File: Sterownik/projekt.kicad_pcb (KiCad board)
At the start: 2 copper layers, 55.9 x 45.7 mm, 61 parts, among them P1 CONN_01X08, P3 CONN_01X05, P4 CONN_01X02, P5 CONN_01X02, P6 USB_OTG, P8 CONN_01X02, SW1 SW_PUSH_SMALL, T10 Si2323DS, T12 2N7002, T18 2N7002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

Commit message: More fixes and new trace placing
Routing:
- net MAIN_VOL: track 62.5 -> 48.2 mm
- net VBUS: track 110.1 -> 119.5 mm
- net GND: track 744.3 -> 740.8 mm, vias 136 -> 138
- net CHARGE_STAT: track 31.8 -> 28.8 mm
- net VDD: track 211.6 -> 214.1 mm
- net CHARGE_ENABLE: track 32.2 -> 32.9 mm

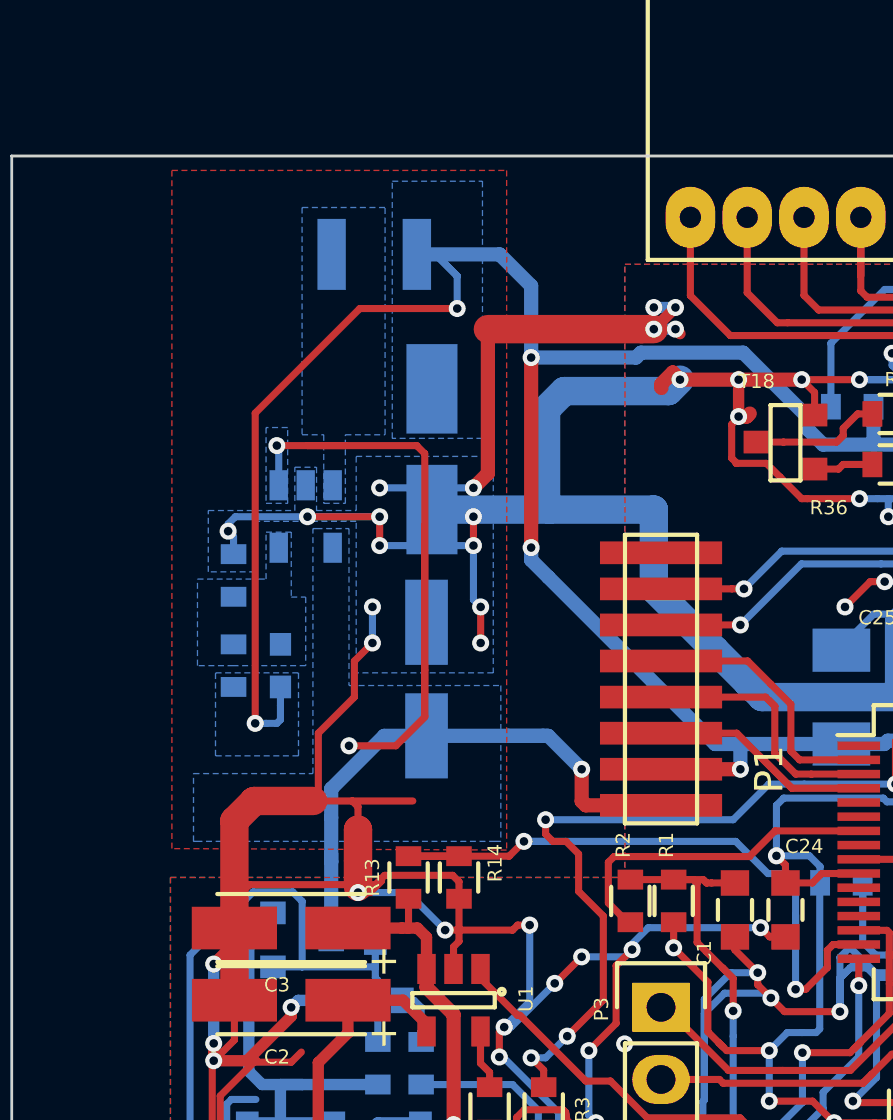
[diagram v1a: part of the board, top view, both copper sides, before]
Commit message: DC/DC converter to linear converter change
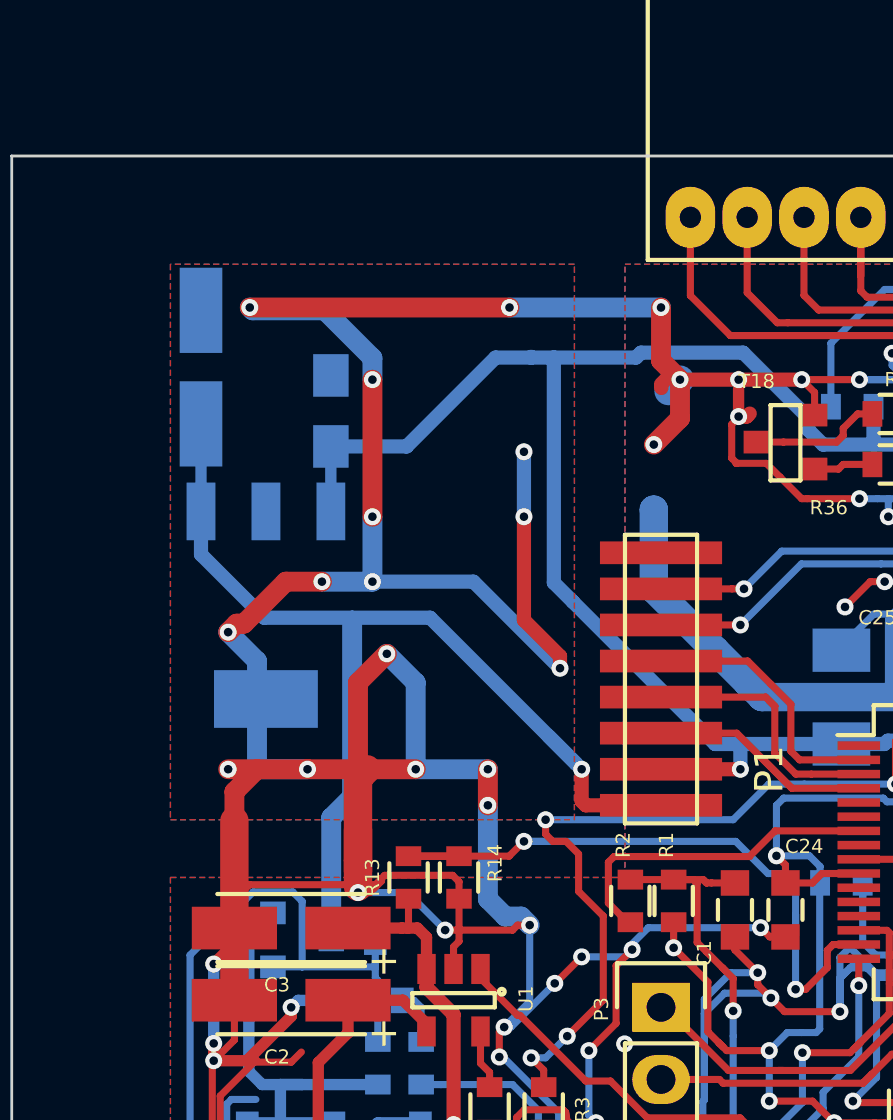
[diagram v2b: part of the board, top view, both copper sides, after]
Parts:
- removed C5: 22p, Capacitors_SMD:C_0603
- removed L2: NLCV32T-1R0M-PF, Capacitors_SMD:C_1210
- removed R18: 300K, Resistors_SMD:R_0603
- removed R20: 1,35M, Resistors_SMD:R_0603
- C6: value 10u -> 1U; footprint Capacitors_Tantalum_SMD:TantalC_SizeB_EIA-3528_HandSoldering -> Capacitors_SMD:C_0805_HandSoldering
- U3: value LT3406 -> MCP1825; footprint Housings_SOT-23_SOT-143_TSOT-6:SOT-23-5 -> SMD_Packages:SOT-223
- moved C4 13.6 mm to (184.5, 87.6)
- moved C6 3.81 mm to (189.0, 89.1), turned to 90 degrees
- moved U3 3.42 mm to (186.8, 96.0), turned to 0 degrees
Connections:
- net VINPUT renamed VON
- U3 pad 3: Net-(L2-Pad1) -> VDD
- U3 pad 4: MAIN_VOL -> GND
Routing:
- net VDD: track 214.1 -> 191.8 mm, vias 15 -> 11
- net GND: track 740.8 -> 759.2 mm, vias 138 -> 140
- net MAIN_VOL: track 48.2 -> 42.7 mm, vias 3 -> 1
- removed copper zone on B.Cu, net MAIN_VOL
- removed copper zone on B.Cu, net Net-(C5-Pad2)
- removed copper zone on B.Cu, net Net-(L2-Pad1)
- removed copper zone on B.Cu, net VDD

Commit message: Ground plane and license.
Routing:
- net GND: track 759.2 -> 717.9 mm, vias 140 -> 136
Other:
- board text added: "EkoPuszka"
- board text added: "SK 2015"
- board text added: "Sławomir Kozok"
- board text added: "Sławomir Kozok 2015"
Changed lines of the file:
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@@
     (links 142)
     (no_connects 0)
-    (area 143.130001 70.020999 255.65 142.527001)
+    (area 177.749999 80.086999 233.730001 125.907001)
     (thickness 1.6)
-    (drawings 9)
-    (tracks 1515)
+    (drawings 13)
+    (tracks 1489)
     (zones 0)
     (modules 57)
@@
     )
   )
+  (gr_text "Sławomir Kozok 2015" (at 181.759896 103.66759 90) (layer F.Cu)
+    (effects (font (size 1 1) (thickness 0.2)))
+  )
+  (gr_text EkoPuszka (at 181.781813 98.566125 90) (layer B.Cu)
+    (effects (font (size 1 1) (thickness 0.25)) (justify mirror))
+  )
+  (gr_text "SK 2015" (at 190.939295 84.888324) (layer B.Cu)
+    (effects (font (size 1 1) (thickness 0.25)) (justify mirror))
+  )
+  (gr_text "Sławomir\nKozok" (at 209.271351 121.92) (layer B.Cu)
+    (effects (font (size 1 1) (thickness 0.25)) (justify mirror))
+  )
   (dimension 22.86 (width 0.3) (layer Cmts.User)
     (gr_text "22,860 mm" (at 149.78 91.567 90) (layer Cmts.User)
@@
   (segment (start 186.182 85.471) (end 195.326 85.471) (width 0.7) (layer F.Cu) (net 1))
   (via (at 195.326 85.471) (size 0.6) (drill 0.3) (layers F.Cu B.Cu) (net 1))
-  (segment (start 190.5 87.249) (end 188.82125 85.57025) (width 0.7) (layer B.Cu) (net 1))
-  (segment (start 188.82125 85.57025) (end 186.28125 85.57025) (width 0.7) (layer B.Cu) (net 1))
   (via (at 186.182 85.471) (size 0.6) (drill 0.3) (layers F.Cu B.Cu) (net 1))
   (segment (start 186.28125 85.57025) (end 186.182 85.471) (width 0.7) (layer B.Cu) (net 1))
@@
   (segment (start 213.233 121.495736) (end 213.233 120.566264) (width 0.25) (layer B.Cu) (net 1))
   (segment (start 213.233 120.566264) (end 213.233 120.142) (width 0.25) (layer B.Cu) (net 1))
-  (segment (start 213.106 123.063) (end 214.376 123.063) (width 0.25) (layer F.Cu) (net 1))
   (via (at 214.376 123.063) (size 0.6) (drill 0.3) (layers F.Cu B.Cu) (net 1))
-  (segment (start 211.836 123.043011) (end 213.086011 123.043011) (width 0.25) (layer B.Cu) (net 1))
-  (segment (start 213.086011 123.043011) (end 213.106 123.063) (width 0.25) (layer B.Cu) (net 1))
-  (via (at 213.106 123.063) (size 0.6) (drill 0.3) (layers F.Cu B.Cu) (net 1))
   (segment (start 205.934989 122.868011) (end 211.661 122.868011) (width 0.25) (layer F.Cu) (net 1))
   (segment (start 211.661 122.868011) (end 211.836 123.043011) (width 0.25) (layer F.Cu) (net 1))
-  (via (at 211.836 123.043011) (size 0.6) (drill 0.3) (layers F.Cu B.Cu) (net 1))
   (segment (start 198.374 122.809) (end 198.673999 123.108999) (width 0.25) (layer F.Cu) (net 1))
   (segment (start 205.694001 123.108999) (end 205.934989 122.868011) (width 0.25) (layer F.Cu) (net 1))
@@
   (via (at 210.185 104.170281) (size 0.6) (drill 0.3) (layers F.Cu B.Cu) (net 1))
   (segment (start 206.506001 116.265999) (end 206.571001 116.200999) (width 0.25) (layer B.Cu) (net 1))
-  (segment (start 206.7706 120.84601) (end 212.183992 120.84601) (width 0.25) (layer B.Cu) (net 1))
   (segment (start 209.581001 109.046999) (end 208.246901 109.046999) (width 0.25) (layer B.Cu) (net 1))
-  (segment (start 212.183992 120.84601) (end 213.096001 119.934001) (width 0.25) (layer B.Cu) (net 1))
   (segment (start 213.096001 119.333999) (end 212.771001 119.008999) (width 0.25) (layer B.Cu) (net 1))
   (segment (start 213.096001 119.934001) (end 213.096001 119.333999) (width 0.25) (layer B.Cu) (net 1))
-  (segment (start 212.170999 119.008999) (end 211.234008 119.94599) (width 0.25) (layer B.Cu) (net 1))
   (segment (start 212.771001 119.008999) (end 212.170999 119.008999) (width 0.25) (layer B.Cu) (net 1))
-  (segment (start 211.234008 119.94599) (end 207.1434 119.94599) (width 0.25) (layer B.Cu) (net 1))
   (segment (start 207.321899 108.721999) (end 206.9592 109.084698) (width 0.25) (layer B.Cu) (net 1))
-  (segment (start 207.1434 119.94599) (end 206.506001 119.308591) (width 0.25) (layer B.Cu) (net 1))
   (segment (start 206.571001 116.200999) (end 209.186503 116.200999) (width 0.25) (layer B.Cu) (net 1))
   (segment (start 208.246901 109.046999) (end 207.921901 108.721999) (width 0.25) (layer B.Cu) (net 1))
@@
   (segment (start 202.1332 116.459) (end 202.1332 113.42618) (width 0.25) (layer B.Cu) (net 1))
   (segment (start 202.1332 113.42618) (end 202.184 113.37538) (width 0.25) (layer B.Cu) (net 1))
-  (segment (start 207.4164 119.507) (end 206.756 118.8466) (width 0.25) (layer F.Cu) (net 1))
-  (segment (start 206.756 118.8466) (end 206.756 116.967) (width 0.25) (layer F.Cu) (net 1))
-  (via (at 206.756 116.967) (size 0.6) (drill 0.3) (layers F.Cu B.Cu) (net 1))
-  (segment (start 205.3336 120.4722) (end 205.70741 120.84601) (width 0.25) (layer B.Cu) (net 1))
-  (segment (start 205.70741 120.84601) (end 212.183992 120.84601) (width 0.25) (layer B.Cu) (net 1))
-  (segment (start 211.234008 119.94599) (end 207.85539 119.94599) (width 0.25) (layer B.Cu) (net 1))
-  (segment (start 207.85539 119.94599) (end 207.4164 119.507) (width 0.25) (layer B.Cu) (net 1))
-  (via (at 207.4164 119.507) (size 0.6) (drill 0.3) (layers F.Cu B.Cu) (net 1))
   (segment (start 203.8604 118.745) (end 203.8604 118.999) (width 0.25) (layer F.Cu) (net 1))
   (segment (start 203.8604 118.999) (end 205.3336 120.4722) (width 0.25) (layer F.Cu) (net 1))
@@
   (segment (start 212.532 111.633) (end 212.532 112.383) (width 0.25) (layer B.Cu) (net 1))
   (segment (start 212.532 112.383) (end 212.471 112.444) (width 0.25) (layer B.Cu) (net 1))
-  (segment (start 210.82 119.507) (end 210.520001 119.806999) (width 0.25) (layer B.Cu) (net 1))
-  (segment (start 207.004409 119.806999) (end 206.576999 119.379589) (width 0.25) (layer B.Cu) (net 1))
-  (segment (start 210.520001 119.806999) (end 207.004409 119.806999) (width 0.25) (layer B.Cu) (net 1))
   (segment (start 206.576999 116.130001) (end 206.756 115.951) (width 0.25) (layer B.Cu) (net 1))
   (segment (start 206.576999 119.379589) (end 206.576999 116.130001) (width 0.25) (layer B.Cu) (net 1))
   (via (at 206.756 115.951) (size 0.6) (drill 0.3) (layers F.Cu B.Cu) (net 1))
-  (segment (start 207.822489 119.266001) (end 206.548591 119.266001) (width 0.25) (layer B.Cu) (net 1))
   (segment (start 206.548591 119.266001) (end 206.506001 119.223411) (width 0.25) (layer B.Cu) (net 1))
   (segment (start 206.506001 119.223411) (end 206.506001 116.265999) (width 0.25) (layer B.Cu) (net 1))
   (segment (start 206.506001 116.265999) (end 206.441001 116.200999) (width 0.25) (layer B.Cu) (net 1))
   (segment (start 206.629 119.253002) (end 206.641999 119.266001) (width 0.25) (layer B.Cu) (net 1))
-  (segment (start 206.641999 119.266001) (end 207.822489 119.266001) (width 0.25) (layer B.Cu) (net 1))
   (segment (start 210.82 119.507) (end 210.37432 119.507) (width 0.25) (layer B.Cu) (net 1))
   (segment (start 210.37432 119.507) (end 210.234309 119.647011) (width 0.25) (layer B.Cu) (net 1))
@@
   (segment (start 219.338999 99.323999) (end 222.123 102.108) (width 0.25) (layer B.Cu) (net 3))
   (segment (start 222.123 102.108) (end 222.123 102.61459) (width 0.25) (layer B.Cu) (net 3))
-  (segment (start 196.088 87.207233) (end 196.088 87.23301) (width 0.5) (layer B.Cu) (net 3))
   (segment (start 204.978 102.743) (end 208.483167 102.743) (width 0.25) (layer B.Cu) (net 3))
   (segment (start 208.483167 102.743) (end 208.614999 102.874832) (width 0.25) (layer B.Cu) (net 3))

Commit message: License, PCB update.
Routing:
- net VDD: track 191.8 -> 195.0 mm
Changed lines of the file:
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@@
     (links 142)
     (no_connects 0)
-    (area 177.749999 80.086999 233.730001 125.907001)
+    (area 143.130001 70.020999 255.65 142.527001)
     (thickness 1.6)
     (drawings 13)
-    (tracks 1489)
+    (tracks 1493)
     (zones 0)
     (modules 57)
@@
   )
   (setup
-    (last_trace_width 0.25)
+    (last_trace_width 0.5)
     (user_trace_width 0.4)
     (user_trace_width 0.5)
@@
   (segment (start 192.404467 107.638779) (end 192.084467 107.318779) (width 0.25) (layer F.Cu) (net 2))
   (segment (start 189.659467 107.297759) (end 189.638447 107.318779) (width 0.25) (layer F.Cu) (net 2))
-  (segment (start 196.886048 87.23301) (end 196.088 87.23301) (width 0.5) (layer B.Cu) (net 3))
-  (segment (start 199.780818 87.23301) (end 196.886048 87.23301) (width 0.5) (layer B.Cu) (net 3))
-  (segment (start 197.557952 95.830952) (end 202.565 100.838) (width 0.5) (layer B.Cu) (net 3))
-  (segment (start 196.886048 87.23301) (end 196.886048 95.159048) (width 0.5) (layer B.Cu) (net 3))
+  (segment (start 196.886048 95.159048) (end 196.886048 87.060991) (width 0.5) (layer B.Cu) (net 3))
+  (segment (start 203.488791 100.838) (end 202.565 100.838) (width 0.5) (layer B.Cu) (net 3))
   (segment (start 196.886048 95.159048) (end 197.557952 95.830952) (width 0.5) (layer B.Cu) (net 3))
+  (segment (start 197.557952 95.830952) (end 202.565 100.838) (width 0.5) (layer B.Cu) (net 3))
+  (segment (start 196.85 87.122) (end 196.85 87.060991) (width 0.5) (layer B.Cu) (net 3))
+  (segment (start 196.85 87.097039) (end 196.85 87.122) (width 0.5) (layer B.Cu) (net 3))
+  (segment (start 196.886048 87.060991) (end 196.85 87.097039) (width 0.5) (layer B.Cu) (net 3))
+  (segment (start 202.311 87.060991) (end 196.85 87.060991) (width 0.5) (layer B.Cu) (net 3))
+  (segment (start 196.85 87.060991) (end 195.006009 87.060991) (width 0.5) (layer B.Cu) (net 3))
+  (segment (start 195.006009 87.060991) (end 194.437 87.63) (width 0.5) (layer B.Cu) (net 3))
+  (segment (start 194.437 87.63) (end 194.83399 87.23301) (width 0.5) (layer B.Cu) (net 3))
   (segment (start 189.036507 90.36323) (end 191.70377 90.36323) (width 0.5) (layer B.Cu) (net 3))
-  (segment (start 191.70377 90.36323) (end 194.83399 87.23301) (width 0.5) (layer B.Cu) (net 3))
-  (segment (start 194.83399 87.23301) (end 196.088 87.23301) (width 0.5) (layer B.Cu) (net 3))
+  (segment (start 191.70377 90.36323) (end 194.437 87.63) (width 0.5) (layer B.Cu) (net 3))
   (segment (start 189.036507 90.36323) (end 189.036507 92.64923) (width 0.4) (layer B.Cu) (net 3))
   (segment (start 208.5445 114.173) (end 208.173731 114.173) (width 0.25) (layer F.Cu) (net 3))
@@
   (segment (start 209.212192 115.80579) (end 212.14675 115.80579) (width 0.25) (layer F.Cu) (net 3))
   (segment (start 212.1408 115.81174) (end 212.14675 115.80579) (width 0.25) (layer F.Cu) (net 3))
-  (segment (start 202.565 100.838) (end 203.488791 100.838) (width 0.5) (layer B.Cu) (net 3))
   (segment (start 203.488791 100.838) (end 207.01 100.838) (width 0.5) (layer B.Cu) (net 3))
   (segment (start 203.454 101.727) (end 203.454 100.872791) (width 0.5) (layer B.Cu) (net 3))
@@
   (segment (start 200.66 101.727) (end 203.454 101.727) (width 0.5) (layer F.Cu) (net 3))
   (via (at 203.454 101.727) (size 0.6) (drill 0.3) (layers F.Cu B.Cu) (net 3))
-  (segment (start 199.952837 87.060991) (end 203.551483 87.060991) (width 0.5) (layer B.Cu) (net 3))
-  (segment (start 199.952837 87.060991) (end 199.780818 87.23301) (width 0.5) (layer B.Cu) (net 3))
+  (segment (start 199.952837 87.060991) (end 202.311 87.060991) (width 0.5) (layer B.Cu) (net 3))
+  (segment (start 202.311 87.060991) (end 203.551483 87.060991) (width 0.5) (layer B.Cu) (net 3))
   (segment (start 205.840999 89.773501) (end 206.364498 90.297) (width 0.5) (layer B.Cu) (net 3))
   (segment (start 203.551483 87.060991) (end 205.840999 89.350507) (width 0.5) (layer B.Cu) (net 3))
@@
   (segment (start 216.5719 93.196196) (end 216.5719 98.948) (width 0.25) (layer F.Cu) (net 28))
   (segment (start 218.06451 97.5401) (end 217.971912 97.447502) (width 0.25) (layer F.Cu) (net 29))
+  (segment (start 217.971912 93.7854) (end 218.300552 93.45676) (width 0.25) (layer F.Cu) (net 29))
+  (segment (start 217.971912 97.447502) (end 217.971912 93.7854) (width 0.25) (layer F.Cu) (net 29))
   (segment (start 218.06451 99.19251) (end 218.06451 97.5401) (width 0.25) (layer F.Cu) (net 29))
   (segment (start 219.0219 100.1499) (end 218.06451 99.19251) (width 0.25) (layer F.Cu) (net 29))
@@
   (segment (start 216.567999 83.170999) (end 216.567999 83.598999) (width 0.25) (layer F.Cu) (net 29))
   (segment (start 218.300552 92.799155) (end 218.300552 93.056187) (width 0.25) (layer F.Cu) (net 29))
-  (segment (start 217.971912 97.447502) (end 217.971912 93.7854) (width 0.25) (layer F.Cu) (net 29))
-  (segment (start 217.971912 93.7854) (end 218.300552 93.45676) (width 0.25) (layer F.Cu) (net 29))
   (segment (start 218.300552 93.45676) (end 218.300552 92.799155) (width 0.25) (layer F.Cu) (net 29))
   (segment (start 218.948 84.836) (end 208.534 84.836) (width 0.25) (layer B.Cu) (net 29))

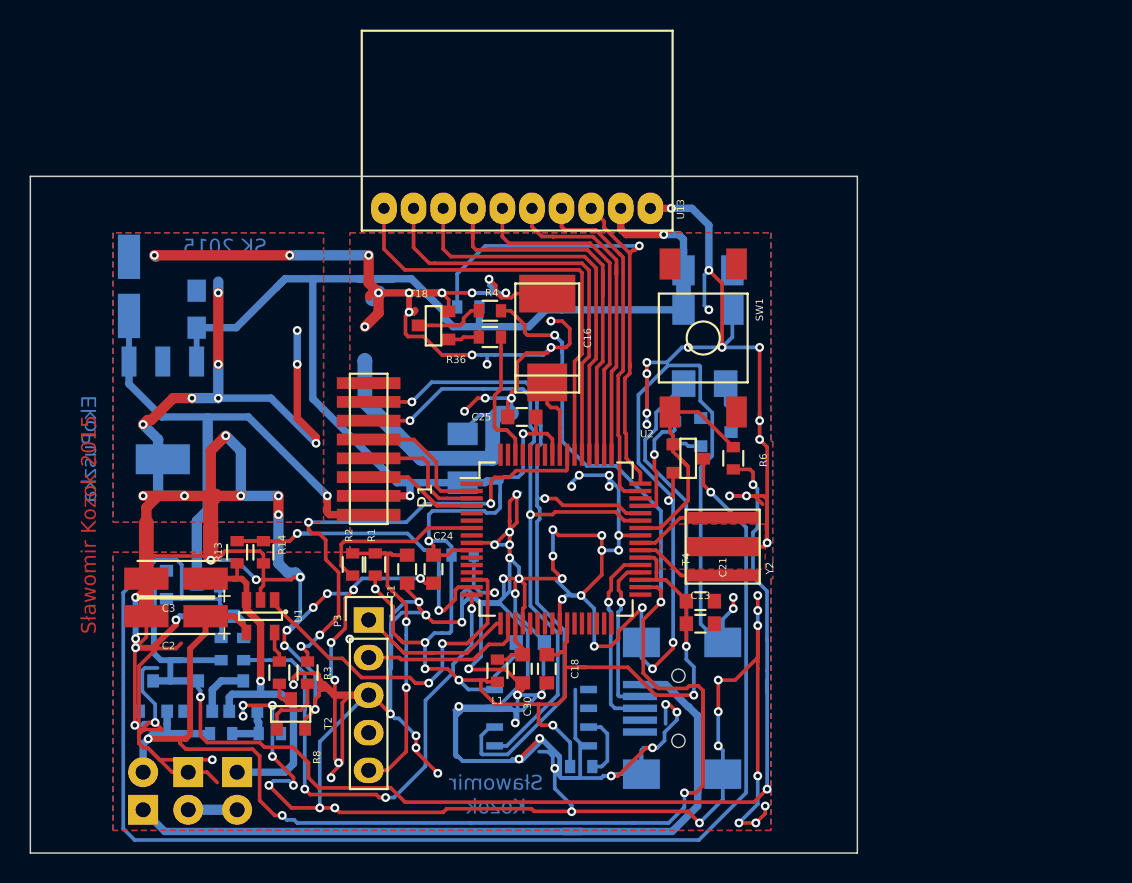
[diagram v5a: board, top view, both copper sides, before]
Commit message: Change board sizes.
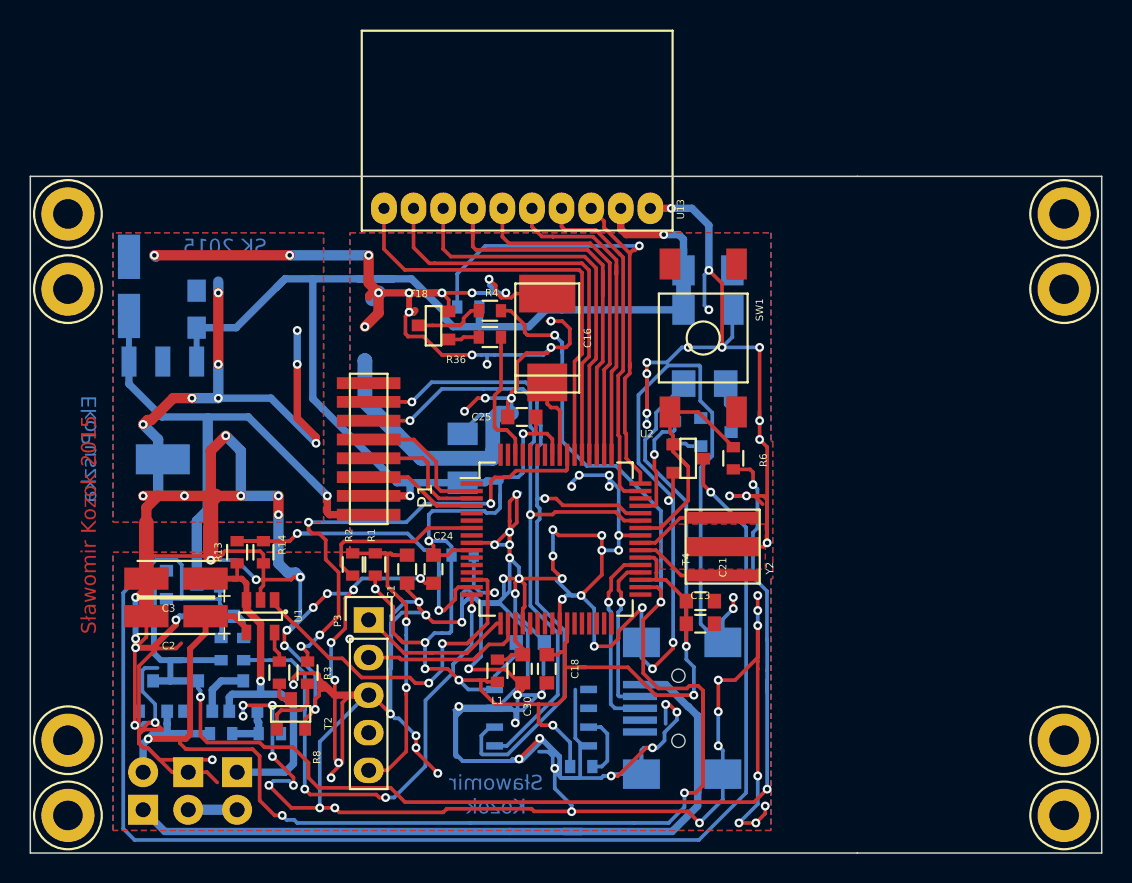
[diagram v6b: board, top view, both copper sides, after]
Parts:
- added REF**: 1pin, Connect:1pin, F.Cu at (180.3, 123.3)
- added REF**: 1pin, Connect:1pin, F.Cu at (180.3, 118.2)
- added REF**: 1pin, Connect:1pin, F.Cu at (180.3, 82.7)
- added REF**: 1pin, Connect:1pin, F.Cu at (180.3, 87.8)
- added REF**: 1pin, Connect:1pin, F.Cu at (247.7, 123.3)
- added REF**: 1pin, Connect:1pin, F.Cu at (247.7, 118.2)
- added REF**: 1pin, Connect:1pin, F.Cu at (247.7, 82.7)
- added REF**: 1pin, Connect:1pin, F.Cu at (247.7, 87.8)
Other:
- board size 55.9 x 45.7 mm -> 72.4 x 45.7 mm
